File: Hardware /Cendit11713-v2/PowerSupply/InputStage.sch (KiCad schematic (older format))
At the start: 13 parts

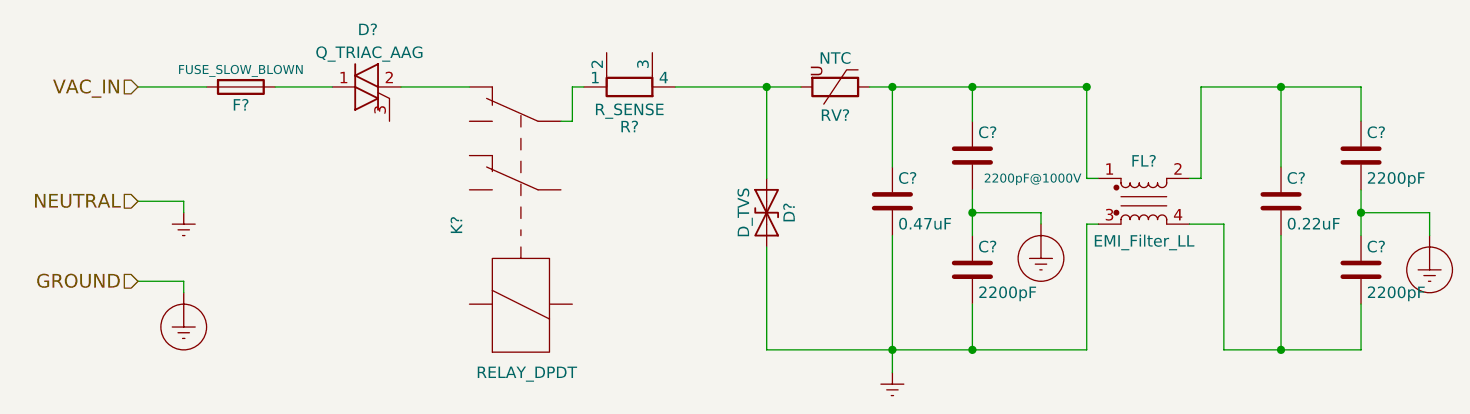
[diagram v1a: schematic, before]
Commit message: Trabajo en Cendit11713 + respaldo de lo hecho hasta hoy
  - Segunda etapa regulador reductor conmutado + LDO
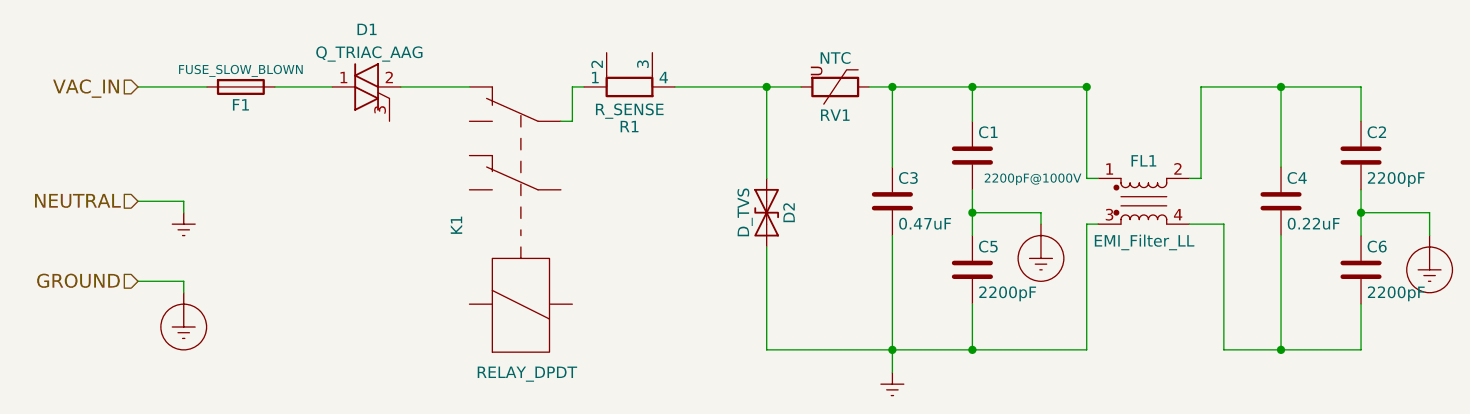
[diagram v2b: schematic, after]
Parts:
- gave numbers to parts that had none: 13
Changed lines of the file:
@@
 $EndDescr
 $Comp
-L EMI_Filter_LL FL?
+L EMI_Filter_LL FL1
 U 1 1 59F21E2B
 P 6050 1900
-F 0 "FL?" H 6050 2075 50  0000 C CNN
+F 0 "FL1" H 6050 2075 50  0000 C CNN
 F 1 "EMI_Filter_LL" H 6050 1725 50  0000 C CNN
 F 2 "" V 6050 1940 50  0000 C CNN
@@
 $EndComp
 $Comp
-L C C?
+L C C3
 U 1 1 59F21EAF
 P 4950 1900
-F 0 "C?" H 4975 2000 50  0000 L CNN
+F 0 "C3" H 4975 2000 50  0000 L CNN
 F 1 "0.47uF" H 4975 1800 50  0000 L CNN
 F 2 "" H 4988 1750 50  0001 C CNN
@@
 $EndComp
 $Comp
-L Fuse F?
+L Fuse F1
 U 1 1 59F21F42
 P 2100 1400
-F 0 "F?" V 2180 1400 50  0000 C CNN
+F 0 "F1" V 2180 1400 50  0000 C CNN
 F 1 "FUSE_SLOW_BLOWN" V 2025 1400 39  0000 C CNN
 F 2 "" V 2030 1400 50  0001 C CNN
@@
 GROUND
 $Comp
-L C C?
+L C C1
 U 1 1 59F222E0
 P 5300 1700
-F 0 "C?" H 5325 1800 50  0000 L CNN
+F 0 "C1" H 5325 1800 50  0000 L CNN
 F 1 "2200pF@1000V" H 5350 1600 39  0000 L CNN
 F 2 "" H 5338 1550 50  0001 C CNN
@@
 $EndComp
 $Comp
-L C C?
+L C C5
 U 1 1 59F22333
 P 5300 2200
-F 0 "C?" H 5325 2300 50  0000 L CNN
+F 0 "C5" H 5325 2300 50  0000 L CNN
 F 1 "2200pF" H 5325 2100 50  0000 L CNN
 F 2 "" H 5338 2050 50  0001 C CNN
@@
 $EndComp
 $Comp
-L Earth_Protective #PWR?
+L Earth_Protective #PWR204
 U 1 1 59F2243C
 P 1850 2300
-F 0 "#PWR?" H 2100 2050 50  0001 C CNN
+F 0 "#PWR204" H 2100 2050 50  0001 C CNN
 F 1 "Earth_Protective" H 2300 2150 50  0001 C CNN
 F 2 "" H 1850 2200 50  0001 C CNN
@@
 $EndComp
 $Comp
-L Earth #PWR?
+L Earth #PWR201
 U 1 1 59F2246E
 P 1850 1950
-F 0 "#PWR?" H 1850 1700 50  0001 C CNN
+F 0 "#PWR201" H 1850 1700 50  0001 C CNN
 F 1 "Earth" H 1850 1800 50  0001 C CNN
 F 2 "" H 1850 1950 50  0001 C CNN
@@
 $EndComp
 $Comp
-L C C?
+L C C4
 U 1 1 59F22618
 P 6650 1900
-F 0 "C?" H 6675 2000 50  0000 L CNN
+F 0 "C4" H 6675 2000 50  0000 L CNN
 F 1 "0.22uF" H 6675 1800 50  0000 L CNN
 F 2 "" H 6688 1750 50  0001 C CNN
@@
 $EndComp
 $Comp
-L C C?
+L C C2
 U 1 1 59F2261E
 P 7000 1700
-F 0 "C?" H 7025 1800 50  0000 L CNN
+F 0 "C2" H 7025 1800 50  0000 L CNN
 F 1 "2200pF" H 7025 1600 50  0000 L CNN
 F 2 "" H 7038 1550 50  0001 C CNN
@@
 $EndComp
 $Comp
-L C C?
+L C C6
 U 1 1 59F22624
 P 7000 2200
-F 0 "C?" H 7025 2300 50  0000 L CNN
+F 0 "C6" H 7025 2300 50  0000 L CNN
 F 1 "2200pF" H 7025 2100 50  0000 L CNN
 F 2 "" H 7038 2050 50  0001 C CNN
@@
 $EndComp
 $Comp
-L Earth #PWR?
+L Earth #PWR205
 U 1 1 59F229EB
 P 4950 2650
-F 0 "#PWR?" H 4950 2400 50  0001 C CNN
+F 0 "#PWR205" H 4950 2400 50  0001 C CNN
 F 1 "Earth" H 4950 2500 50  0001 C CNN
 F 2 "" H 4950 2650 50  0001 C CNN
@@
 $EndComp
 $Comp
-L Earth_Protective #PWR?
+L Earth_Protective #PWR202
 U 1 1 59F22A54
 P 5600 2000
-F 0 "#PWR?" H 5850 1750 50  0001 C CNN
+F 0 "#PWR202" H 5850 1750 50  0001 C CNN
 F 1 "Earth_Protective" H 6050 1850 50  0001 C CNN
 F 2 "" H 5600 1900 50  0001 C CNN
@@
 $EndComp
 $Comp
-L Earth_Protective #PWR?
+L Earth_Protective #PWR203
 U 1 1 59F22AB8
 P 7300 2050
-F 0 "#PWR?" H 7550 1800 50  0001 C CNN
+F 0 "#PWR203" H 7550 1800 50  0001 C CNN
 F 1 "Earth_Protective" H 7750 1900 50  0001 C CNN
 F 2 "" H 7300 1950 50  0001 C CNN
@@
 	6300 1800 6250 1800
 $Comp
-L Varistor RV?
+L Varistor RV1
 U 1 1 59F22F6A
 P 4700 1400
-F 0 "RV?" V 4825 1400 50  0000 C CNN
+F 0 "RV1" V 4825 1400 50  0000 C CNN
 F 1 "NTC" V 4575 1400 50  0000 C CNN
 F 2 "" V 4630 1400 50  0001 C CNN
@@
 $EndComp
 $Comp
-L D_TVS D?
+L D_TVS D2
 U 1 1 59F232D8
 P 4400 1950
-F 0 "D?" H 4400 2050 50  0000 C CNN
+F 0 "D2" H 4400 2050 50  0000 C CNN
 F 1 "D_TVS" H 4400 1850 50  0000 C CNN
 F 2 "" H 4400 1950 50  0001 C CNN
@@
 	4400 2550 5800 2550
 $Comp
-L Q_TRIAC_AAG D?
+L Q_TRIAC_AAG D1
 U 1 1 59F23CBA
 P 2650 1400
-F 0 "D?" V 2900 1350 50  0000 L CNN
+F 0 "D1" V 2900 1350 50  0000 L CNN
 F 1 "Q_TRIAC_AAG" V 2800 1150 50  0000 L CNN
 F 2 "" V 2725 1425 50  0001 C CNN
@@
 $EndComp
 $Comp
-L RELAY-2XCHANGE_DPDT_RevE_Date15jun2010 K?
+L RELAY-2XCHANGE_DPDT_RevE_Date15jun2010 K1
 U 1 1 59F23D7B
 P 3350 2000
-F 0 "K?" H 3345 2305 50  0000 C CNN
+F 0 "K1" H 3345 2305 50  0000 C CNN
 F 1 "RELAY_DPDT" V 2700 2000 50  0000 C CNN
 F 2 "" H 3350 2000 50  0000 C CNN
@@
 $EndComp
 $Comp
-L R_Shunt R?
+L R_Shunt R1
 U 1 1 59F24327
 P 3800 1400
-F 0 "R?" V 3625 1400 50  0000 C CNN
+F 0 "R1" V 3625 1400 50  0000 C CNN
 F 1 "R_SENSE" V 3700 1400 50  0000 C CNN
 F 2 "" V 3730 1400 50  0001 C CNN
